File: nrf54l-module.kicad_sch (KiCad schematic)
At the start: 42 parts, among them SW1 TS24CA, U1 NRF54L15-QFAA-R, U2 XL-0201SURC, U3 TLV62569DBVR, U4 XL-0201SURC, U5 XL-0201SURC, X1 XL7EL89CKI-111YLC-32M

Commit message: chore: refactoring
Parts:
- C1, C12: LCSC Part C19271867 -> C5140319
- L4: value 2.2uF -> 2.2uH
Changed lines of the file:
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@@
 			)
 		)
-		(property "LCSC Part" "C19271867"
+		(property "LCSC Part" "C5140319"
 			(at 68.58 26.67 0)
 			(effects
@@
 			)
 		)
-		(property "LCSC Part" "C19271867"
+		(property "LCSC Part" "C5140319"
+			(at 81.28 26.67 0)
+			(effects
+				(font
+					(size 1.27 1.27)
+				)
+				(hide yes)
+			)
+		)
+		(property "Field6" ""
 			(at 81.28 26.67 0)
 			(effects
@@
 			)
 		)
-		(property "Value" "2.2uF"
+		(property "Value" "2.2uH"
 			(at 215.646 32.766 0)
 			(effects

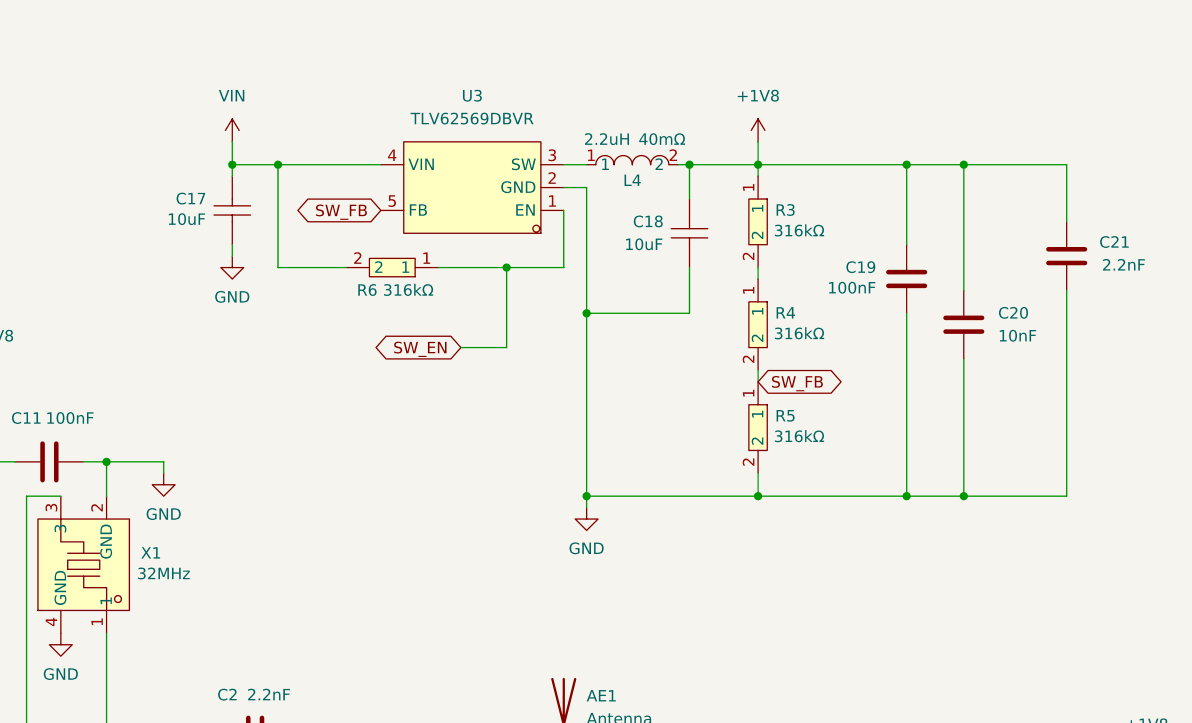
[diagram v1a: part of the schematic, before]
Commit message: bugfix: DRC
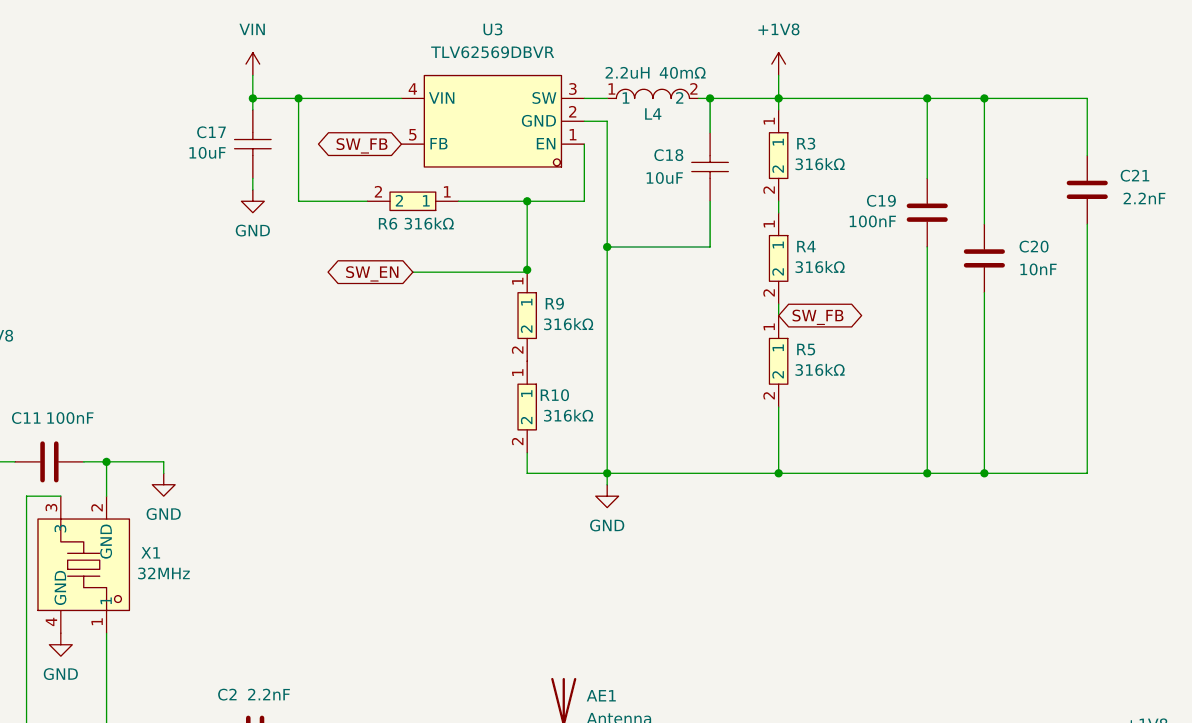
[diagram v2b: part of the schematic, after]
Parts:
- added R10, R9: RC0402FR-07160KL, Resistor_SMD:R_0201_0603Metric, symbol easyeda2kicad:RC0402FR-07160KL
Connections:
- net GND: now also R10.2
- net SW_EN: now also R9.1
- new net: R10.1, R9.2
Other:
- moved on the sheet: C17, C18, C19, C20, C21, L4, R3, R4, R5, R6, U3

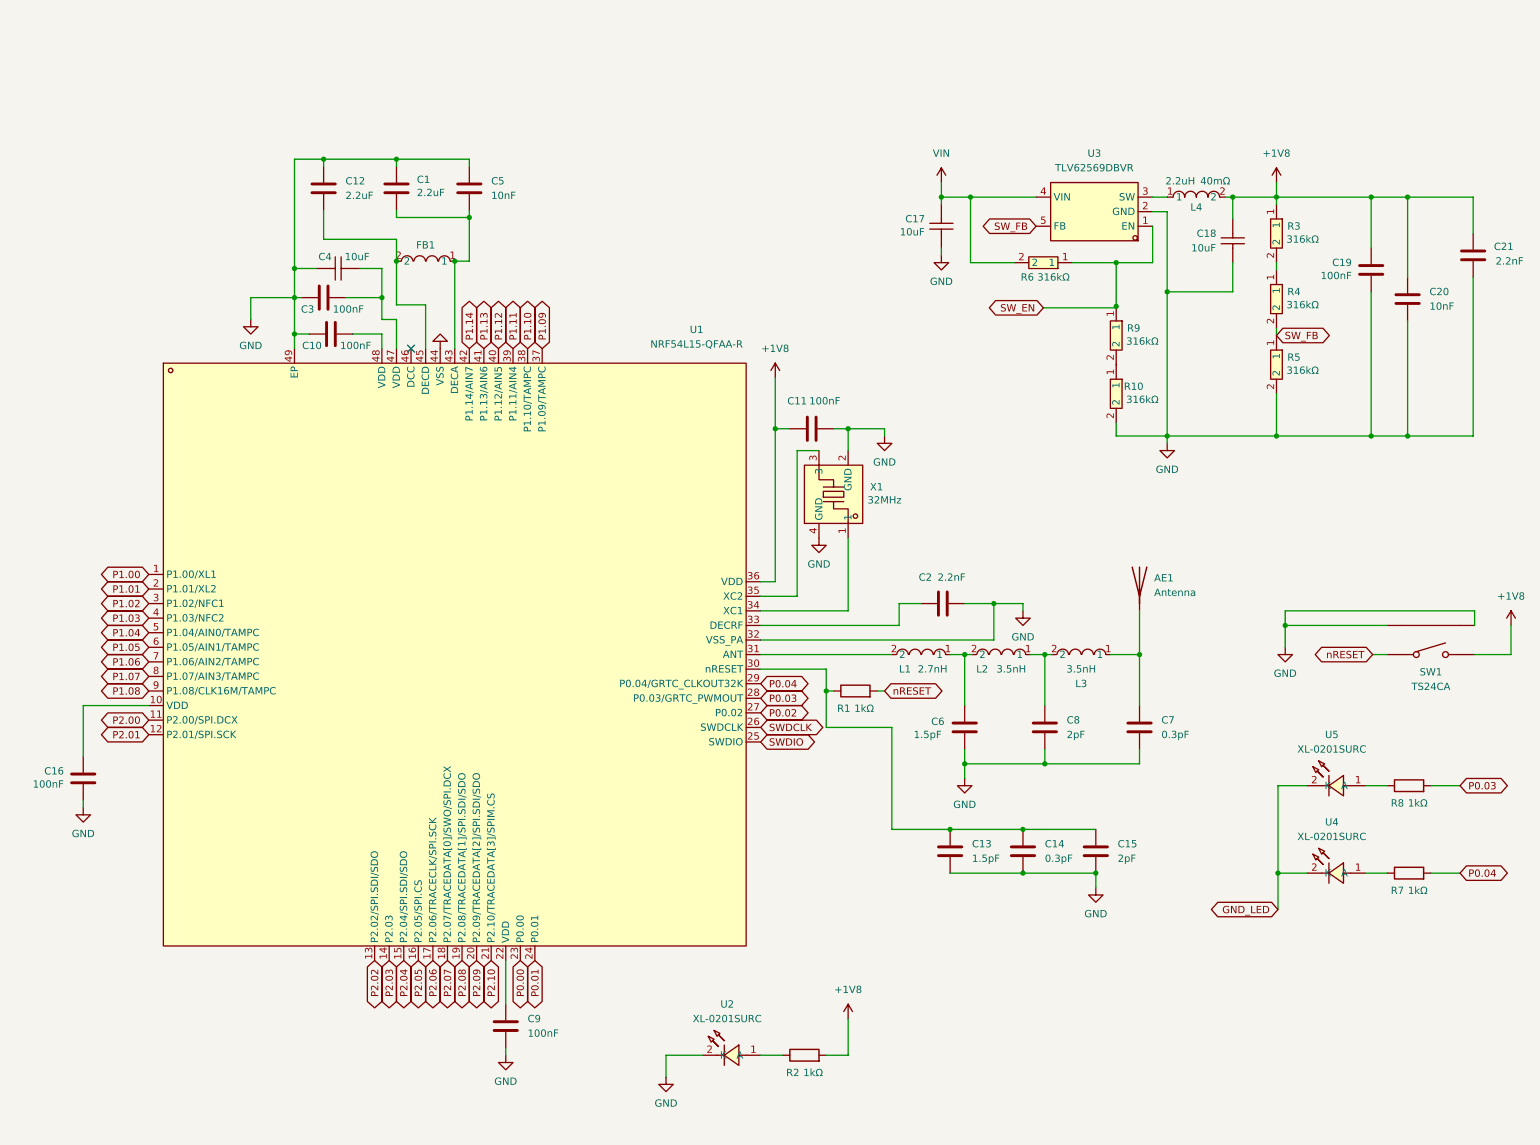
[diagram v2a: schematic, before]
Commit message: feat: 1.27 mm pitch
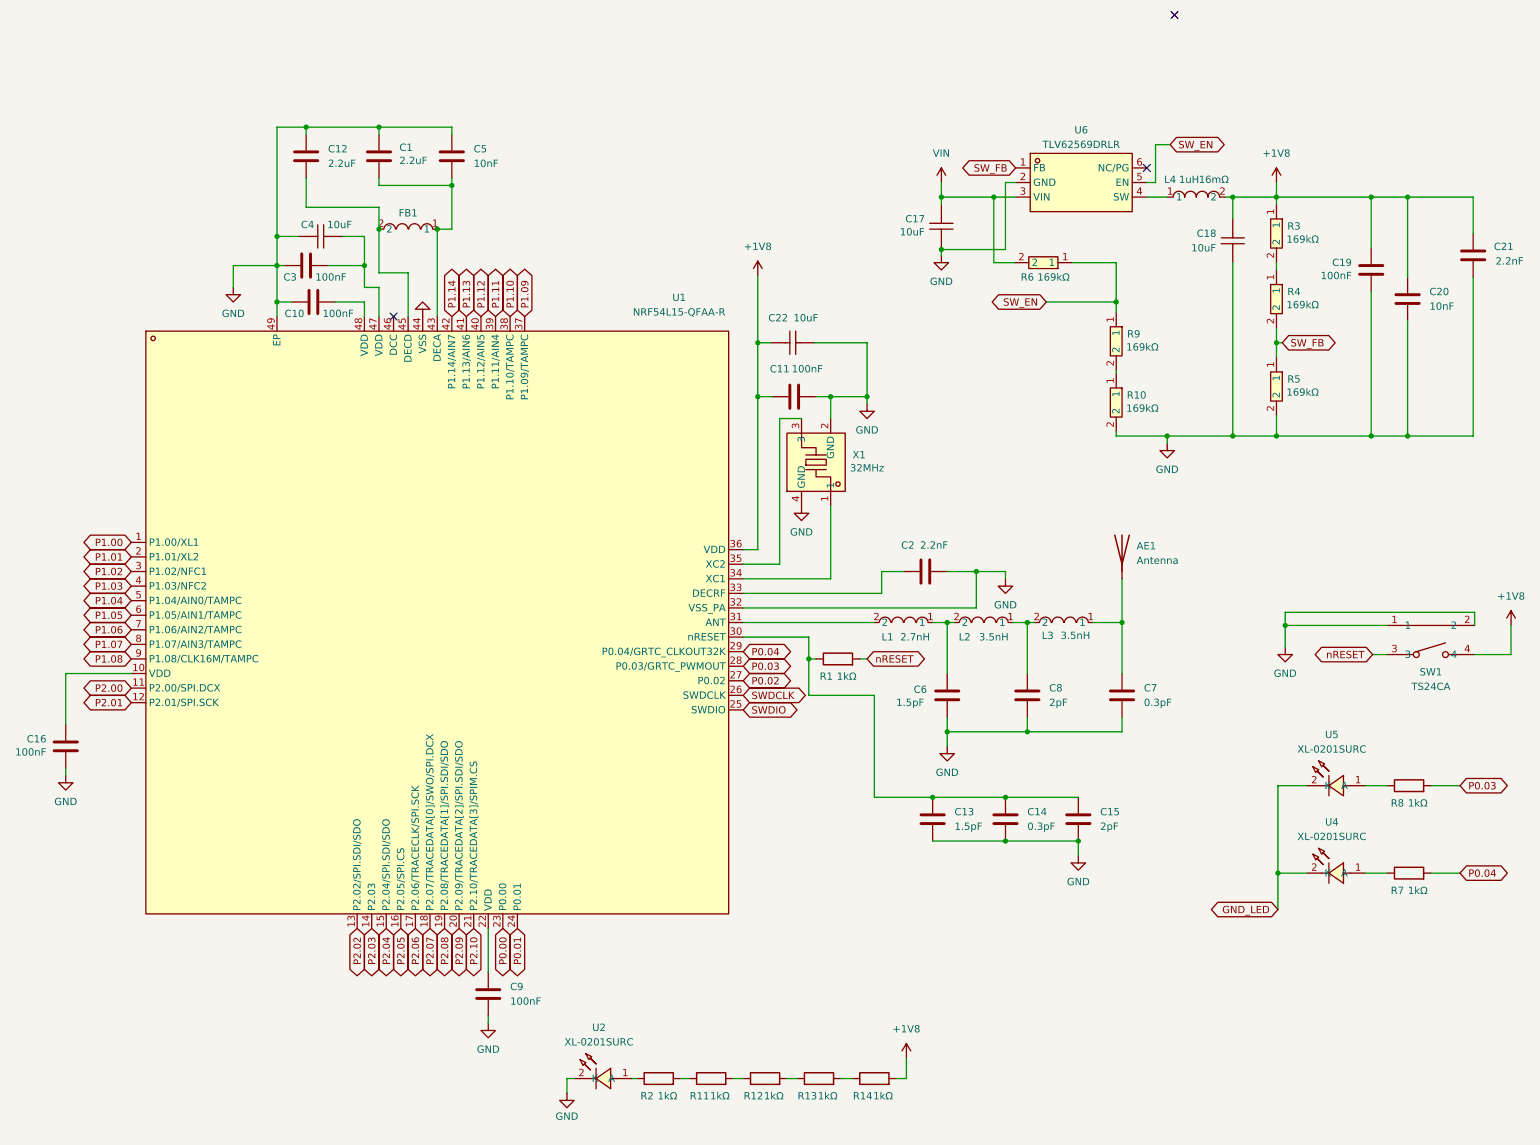
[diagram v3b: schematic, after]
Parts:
- removed L4: 2.2uH, easyeda2kicad:IND-SMD_L3.2-W2.5-LQH32CN1R0M53L, symbol easyeda2kicad:FTC322512S2R2MBCD
- removed U3: TLV62569DBVR, easyeda2kicad:SOT-23-5_L3.0-W1.7-P0.95-LS2.8-BR, symbol easyeda2kicad:TLV62569DBVR
- added C22: 10uF, easyeda2kicad:C0402, symbol easyeda2kicad:GRM155R60J106ME44D
- added L4: 1uH, easyeda2kicad:L1008, symbol easyeda2kicad:FTC252012S1R0MBCD
- added R11, R12, R13, R14: 1kΩ, Resistor_SMD:R_0201_0603Metric, symbol Device:R
- added U6: TLV62569DRLR, easyeda2kicad:SOT-563_L1.6-W1.2-P0.50-LS1.6-BL, symbol easyeda2kicad:TLV62569DRLR
- R10, R3, R4, R5, R6, R9: LCSC Part C240016 -> C166333
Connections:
- net +1V8: now also C22.1, L4.2, R14.2; no longer R2.2
- net GND: now also SW1.2, C22.2, U6.2 (GND); no longer SW1.22 (2)
- net SW_EN: now also U6.5 (EN)
- net SW_FB: now also U6.1 (FB)
- net VIN: now also U6.3 (VIN)
- new net: L4.1, U6.4 (SW)
- new net: R11.1, R2.2
- new net: R13.2, R14.1
- new net: R11.2, R12.1
- new net: R12.2, R13.1
- no-connect marks 1 -> 3
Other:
- moved on the sheet: AE1, C1, C10, C11, C12, C13, C14, C15, C16, C2, C3, C4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

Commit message: feat: additinal button on P1.12
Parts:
- added SW2: TD-1183SN-1.7H-250, easyeda2kicad:KEY-SMD_L3.0-W2.5-LS4.0, symbol easyeda2kicad:TD-1183SN-1.7H-250
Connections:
- net +1V8: now also SW2.1
- net P1.12: now also SW2.2
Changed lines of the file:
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@@
 	(wire
 		(pts
+			(xy 33.528 181.61) (xy 33.528 186.182)
+		)
+		(stroke
+			(width 0)
+			(type default)
+		)
+	)
+	(wire
+		(pts
 			(xy 97.282 155.702) (xy 97.282 163.322)
 		)
@@
 	(wire
 		(pts
+			(xy 33.528 186.182) (xy 40.64 186.182)
+		)
+		(stroke
+			(width 0)
+			(type default)
+		)
+	)
+	(wire
+		(pts
 			(xy 194.564 46.482) (xy 206.756 46.482)
 		)
@@
 	(wire
 		(pts
+			(xy 50.8 186.182) (xy 60.198 186.182)
+		)
+		(stroke
+			(width 0)
+			(type default)
+		)
+	)
+	(wire
+		(pts
 			(xy 163.322 53.594) (xy 163.322 62.992)
 		)
@@
 		)
 	)
+	(global_label "P1.12"
+		(shape bidirectional)
+		(at 60.198 186.182 0)
+		(fields_autoplaced yes)
+		(effects
+			(font
+				(size 1.27 1.27)
+			)
+			(justify left)
+		)
+		(property "Intersheetrefs" "${INTERSHEET_REFS}"
+			(at 69.4011 186.182 0)
+			(effects
+				(font
+					(size 1.27 1.27)
+				)
+				(justify left)
+				(hide yes)
+			)
+		)
+	)
 	(global_label "P1.05"
 		(shape bidirectional)
@@
 	)
 	(symbol
+		(lib_id "easyeda2kicad:TD-1183SN-1.7H-250")
+		(at 45.72 186.182 0)
+		(unit 1)
+		(exclude_from_sim no)
+		(in_bom yes)
+		(on_board yes)
+		(dnp no)
+		(fields_autoplaced yes)
+		(property "Reference" "SW2"
+			(at 45.72 179.07 0)
+			(effects
+				(font
+					(size 1.27 1.27)
+				)
+			)
+		)
+		(property "Value" "TD-1183SN-1.7H-250"
+			(at 45.72 181.61 0)
+			(effects
+				(font
+					(size 1.27 1.27)
+				)
+			)
+		)
+		(property "Footprint" "easyeda2kicad:KEY-SMD_L3.0-W2.5-LS4.0"
+			(at 45.72 193.802 0)
+			(effects
+				(font
+					(size 1.27 1.27)
+				)
+				(hide yes)
+			)
+		)
+		(property "Datasheet" ""
+			(at 45.72 186.182 0)
+			(effects
+				(font
+					(size 1.27 1.27)
+				)
+				(hide yes)
+			)
+		)
+		(property "Description" ""
+			(at 45.72 186.182 0)
+			(effects
+				(font
+					(size 1.27 1.27)
+				)
+				(hide yes)
+			)
+		)
+		(property "LCSC Part" "C2905195"
+			(at 45.72 196.342 0)
+			(effects
+				(font
+					(size 1.27 1.27)
+				)
+				(hide yes)
+			)
+		)
+		(pin "2"
+		)
+		(pin "1"
+		)
+		(instances
+			(project ""
+				(path "/0864898c-5307-44d7-ba2c-a6227ddaacc4"
+					(reference "SW2")
+					(unit 1)
+				)
+			)
+		)
+	)
+	(symbol
 		(lib_id "Device:C")
 		(at 65.532 21.082 0)
@@
 					(unit 1)
 				)
+			)
+		)
+	)
+	(symbol
+		(lib_id "power:+1V8")
+		(at 33.528 181.61 0)
+		(unit 1)
+		(exclude_from_sim no)
+		(in_bom yes)
+		(on_board yes)
+		(dnp no)
+		(fields_autoplaced yes)
+		(property "Reference" "#PWR019"
+			(at 33.528 185.42 0)
+			(effects
+				(font
+					(size 1.27 1.27)
+				)
+				(hide yes)
+			)
+		)
+		(property "Value" "+1V8"
+			(at 33.528 176.53 0)
+			(effects
+				(font
+					(size 1.27 1.27)
+				)
+			)
+		)
+		(property "Footprint" ""
+			(at 33.528 181.61 0)
+			(effects
+				(font
+					(size 1.27 1.27)
+				)
+				(hide yes)
+			)
+		)
+		(property "Datasheet" ""
+			(at 33.528 181.61 0)
+			(effects
+				(font
+					(size 1.27 1.27)
+				)
+				(hide yes)
+			)
+		)
+		(property "Description" "Power symbol creates a global label with name \"+1V8\""
+			(at 33.528 181.61 0)
+			(effects
+				(font
+					(size 1.27 1.27)
+				)
+				(hide yes)
+			)
+		)
+		(pin "1"
+		)
+		(instances
+			(project "nrf54l-module"
+				(path "/0864898c-5307-44d7-ba2c-a6227ddaacc4"
+					(reference "#PWR019")
+					(unit 1)
+				)

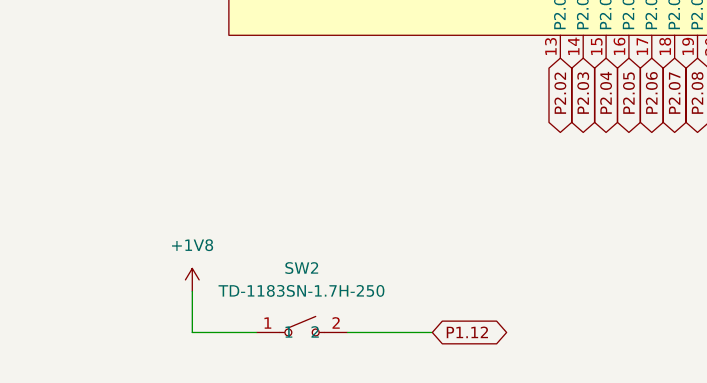
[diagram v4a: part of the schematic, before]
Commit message: feat: 6 layer because it's cheaper lol wtf
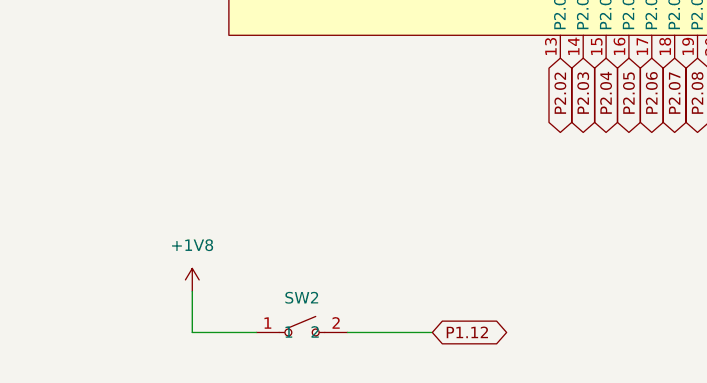
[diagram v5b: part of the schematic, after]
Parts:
- SW2: value TD-1183SN-1.7H-250 -> (none); LCSC Part C2905195 -> C231329
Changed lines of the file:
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@@
 		(on_board yes)
 		(dnp no)
-		(fields_autoplaced yes)
 		(property "Reference" "SW2"
-			(at 45.72 179.07 0)
+			(at 45.72 182.372 0)
 			(effects
 				(font
@@
 			)
 		)
-		(property "Value" "TD-1183SN-1.7H-250"
+		(property "Value" ""
 			(at 45.72 181.61 0)
 			(effects
@@
 					(size 1.27 1.27)
 				)
+				(hide yes)
 			)
 		)
@@
 			)
 		)
-		(property "LCSC Part" "C2905195"
+		(property "LCSC Part" "C231329"
 			(at 45.72 196.342 0)
 			(effects

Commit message: chore: checkpoint
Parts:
- removed C13: 1.5pF, Capacitor_SMD:C_0201_0603Metric, symbol Device:C
- removed C14: 0.3pF, Capacitor_SMD:C_0201_0603Metric, symbol Device:C
- removed SW1: TS24CA, easyeda2kicad:SW-SMD_TS24CA, symbol easyeda2kicad:TS24CA
- added C23: 10uF, easyeda2kicad:C0402, symbol easyeda2kicad:GRM155R60J106ME44D
- added J1: BM28B0.6-10DS/2-0.35V(51), easyeda2kicad:CONN-SMD_BM28B0.6-10DS-2-0.35V-51, symbol easyeda2kicad:BM28B0.6-10DS_2-0.35V(51)
- added R15, R16: 1kΩ, Resistor_SMD:R_0201_0603Metric, symbol Device:R
- added SW1: ~, easyeda2kicad:KEY-SMD_B3U-1000PM, symbol easyeda2kicad:TD-1183SN-1.7H-250
- added U3, U7: XL-0201SURC, easyeda2kicad:LED-SMD_L0.65-W0.35-P0.41_XL-0201SURC, symbol easyeda2kicad:XL-0201SURC
- L2, L3: value LQP03TN3N5B02D -> MLG0603P2N7CT000; LCSC Part C206424 -> C76752
- SW2: value (none) -> ~; footprint easyeda2kicad:KEY-SMD_L3.0-W2.5-LS4.0 -> easyeda2kicad:KEY-SMD_B3U-1000PM
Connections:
- net +1V8: now also C23.1, J1.6, SW1.1
- net GND: now also C23.2, J1.13, J1.14
- net GND_LED: now also R15.1, R16.1
- net P0.02: now also J1.3
- net P0.03: now also J1.2
- net P0.04: now also J1.1
- net P1.09: now also J1.5
- net P1.10: now also J1.4
- net P1.11: now also J1.7
- net P2.05: now also U7.1 (A)
- net P2.06: now also U3.1 (A)
- net SWDCLK: now also J1.10
- net SWDIO: now also J1.9
- net VIN: now also J1.11, J1.12
- net nRESET: now also J1.8, SW1.2
- new net: R15.2, U3.2 (K)
- new net: R16.2, U7.2 (K)
- no-connect marks 3 -> 2
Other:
- moved on the sheet: C15, R7, R8, SW2, U4, U5

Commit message: chore: checkpoint
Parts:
- removed FB1: BLM03PX121SN1D, easyeda2kicad:L0201, symbol easyeda2kicad:BLM03PX121SN1D
- removed R12, R13, R14, R15, R16, R2: 1kΩ, Resistor_SMD:R_0201_0603Metric, symbol Device:R
- removed U2, U3, U4, U5, U7: XL-0201SURC, easyeda2kicad:LED-SMD_L0.65-W0.35-P0.41_XL-0201SURC, symbol easyeda2kicad:XL-0201SURC
- added C11: 2.2uF, Capacitor_SMD:C_0201_0603Metric, symbol Device:C
- added LED1, LED2, LED3, LED4: TZ-P2-0402RTIA1-0.45T, easyeda2kicad:LED0402-RD_RED, symbol easyeda2kicad:TZ-P2-0402RTIA1-0.45T
- added R10: 1kΩ, Resistor_SMD:R_0201_0603Metric, symbol Device:R
- C1: renamed from C12; LCSC Part C5140319 -> C76933
- C2: renamed from C1; LCSC Part C5140319 -> C76933
- renumbered C19 to C10, C20 to C12, C10 to C13, C22 to C14, C11 to C15, C2 to C16, C6 to C17, C8 to C18, C7 to C19, C15 to C20, C16 to C21, C9 to C22, C5 to C3, C17 to C4, C23 to C5, C4 to C6, C18 to C7, C21 to C8, C3 to C9, L4 to L1, L1 to L2, L2 to L3, L3 to L4, R3 to R1, R6 to R2, R4 to R3, R9 to R4, R10 to R6, R8 to R7, R1 to R8, R7 to R9, U6 to U1, U1 to U2
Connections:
- net +1V8: now also C11.2
- net GND: now also C11.1
- net GND_LED: now also LED1.1 (K), LED2.1 (K), LED3.1 (K), LED4.1 (K)
- net P0.00: now also R7.2
- net P0.01: now also R9.2
- net P0.02: no longer J1.3
- net P0.03: no longer J1.2, R7.2
- net P0.04: no longer J1.1, R9.2
- net P1.00: now also R10.2
- net P1.01: now also R11.2
- net P1.05: now also J1.3
- net P1.06: now also J1.4
- net P1.07: now also J1.5
- net P1.09: no longer J1.5
- net P1.10: no longer J1.4
- net P1.11: now also SW2.2; no longer J1.7
- net P1.12: no longer SW2.2
- net P2.02: now also J1.7
- net P2.03: now also J1.2
- net P2.04: now also J1.1
- net at R11.1: now also LED4.2 (A)
- net at R9.1: now also LED2.2 (A)
- net at R7.1: now also LED1.2 (A)
- new net: LED3.2 (A), R10.1
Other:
- moved on the sheet: C10, C12, C20, C4, C7, C8, L1, R1, R2, R3, R4, R5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

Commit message: bugfix(critical): 1.8V power to VDD
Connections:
- net +1V8: now also C13.1, C21.2, C22.1, C6.2, C9.2, U2.10 (VDD), U2.22 (VDD), U2.47 (VDD), U2.48 (VDD)
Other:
- moved on the sheet: C22
